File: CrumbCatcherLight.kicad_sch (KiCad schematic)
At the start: 8 parts, among them J1 USB_C_Receptacle_USB2.0, U1 ECMF02-2AMX6

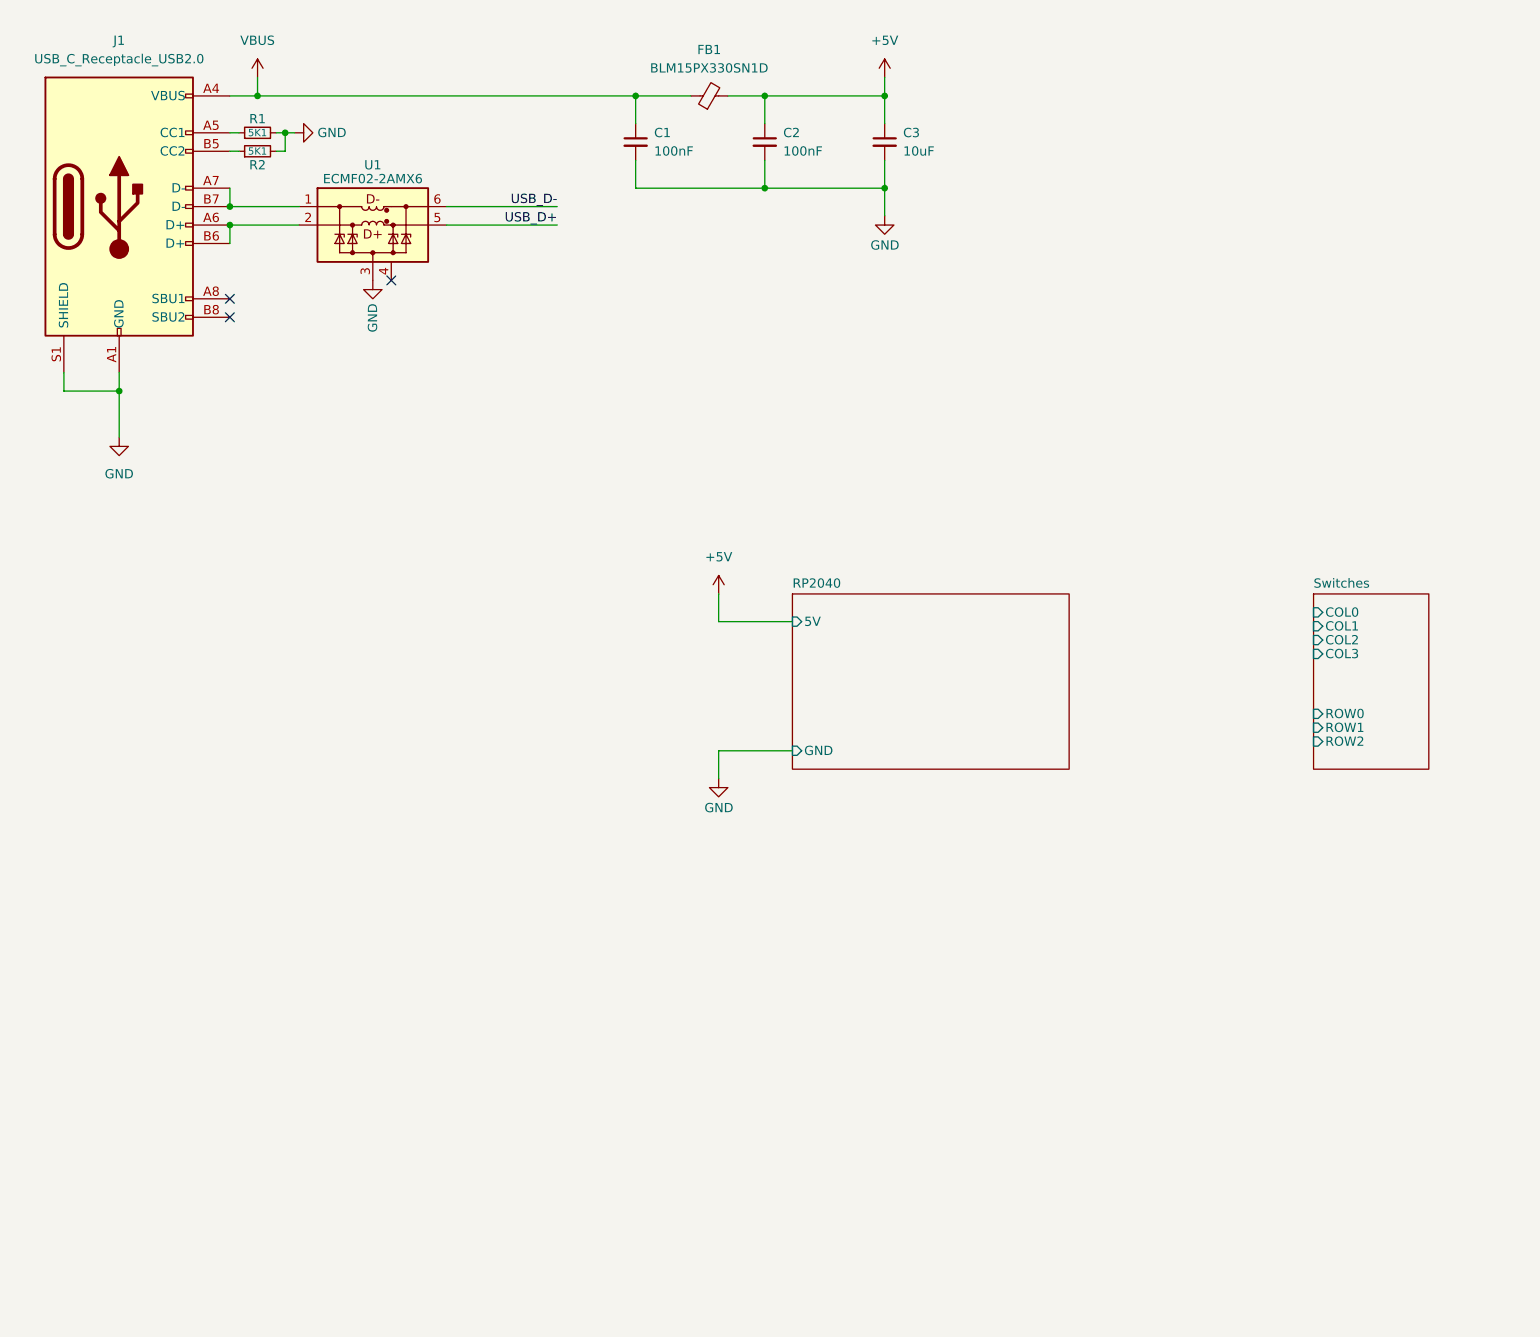
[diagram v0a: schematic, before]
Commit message: Update lib, finish off rotary encoder schematic, reselect diode for reset circuit
Update RP2040, rename bom only footprint, add mechanical footprint. Add PCB symbol
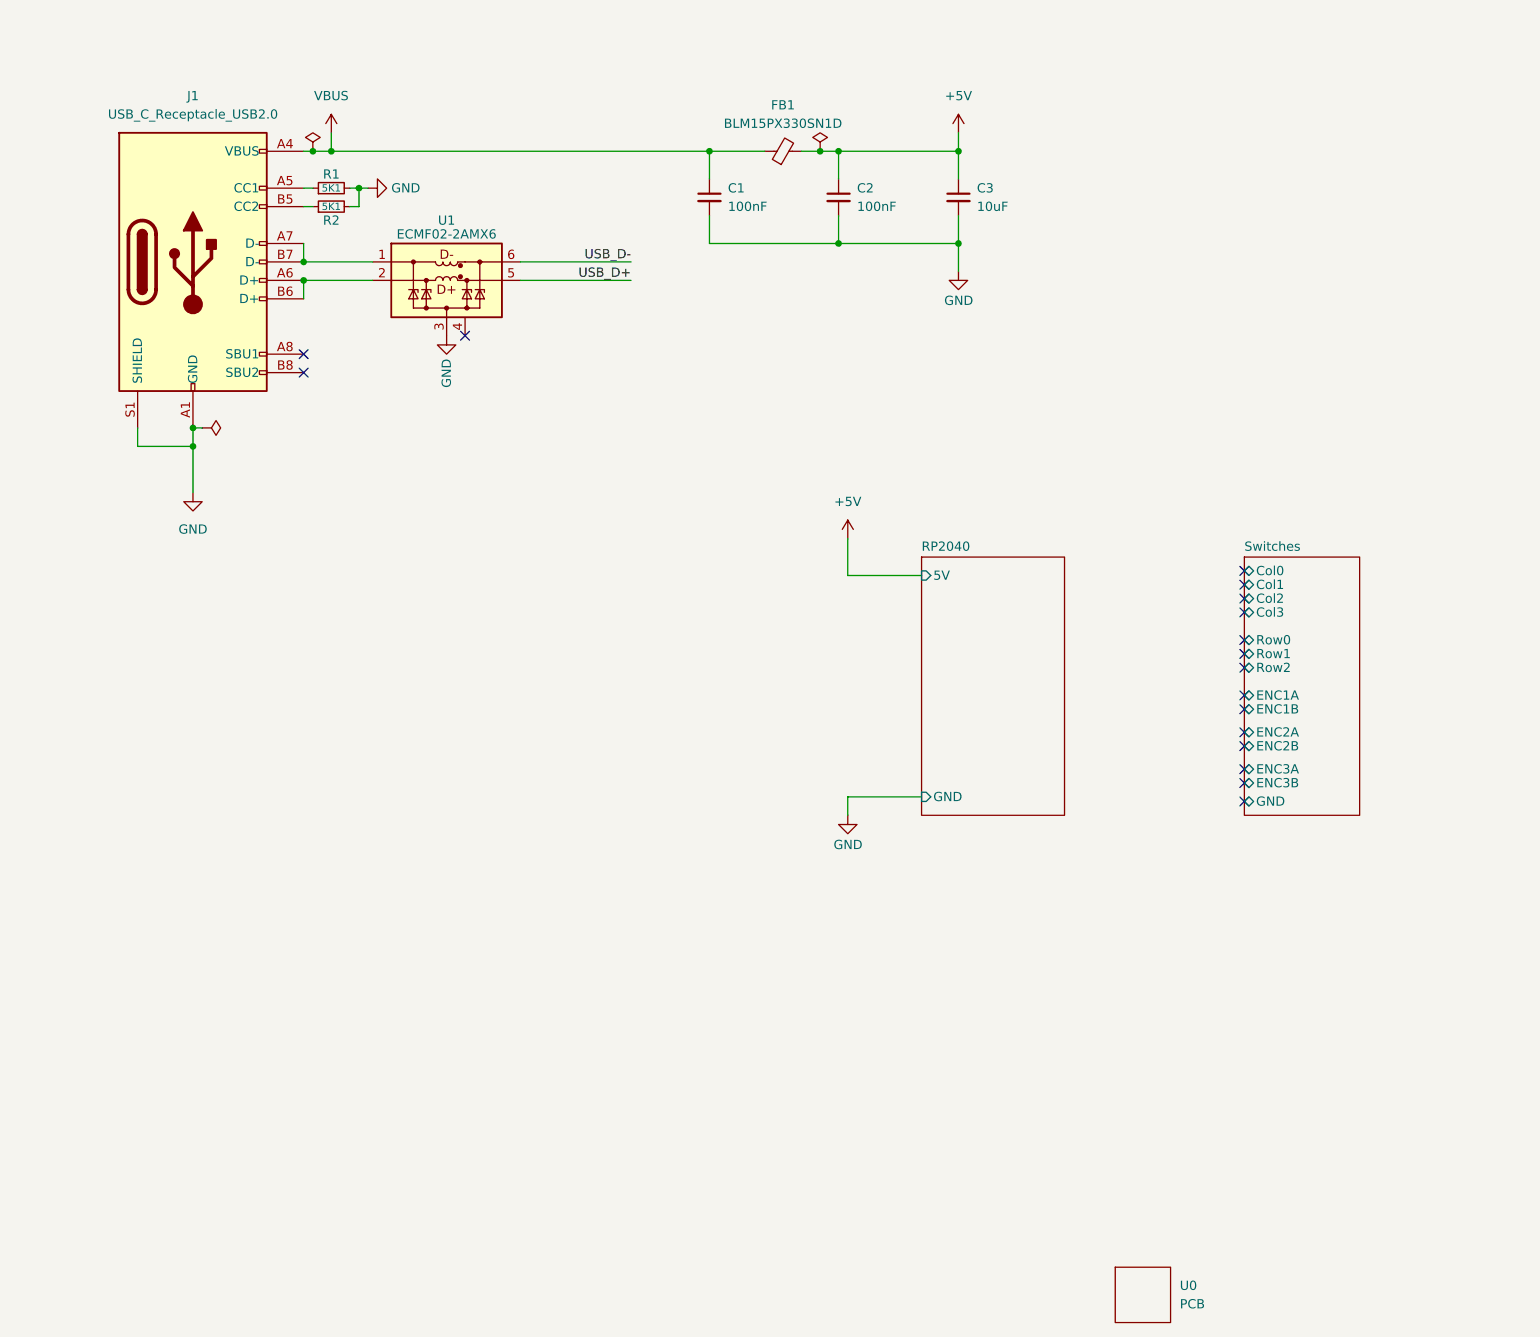
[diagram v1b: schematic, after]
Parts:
- added U0: PCB, Mad_Footprints:BOM, symbol Mad_Symbols:PCB
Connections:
- no-connect marks 3 -> 17
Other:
- sheet Switches ports: added Col0, Col1, Col2, Col3, ENC1A, ENC1B, ENC2A, ENC2B, ENC3A, ENC3B, GND, Row0, Row1, Row2; removed COL0, COL1, COL2, COL3, ROW0, ROW1, ROW2
- moved on the sheet: C1, C2, C3, FB1, J1, R1, R2, U1

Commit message: Finish off rotary encoders, add EMC zone for USB, fix few remaining lib links, fix DRC
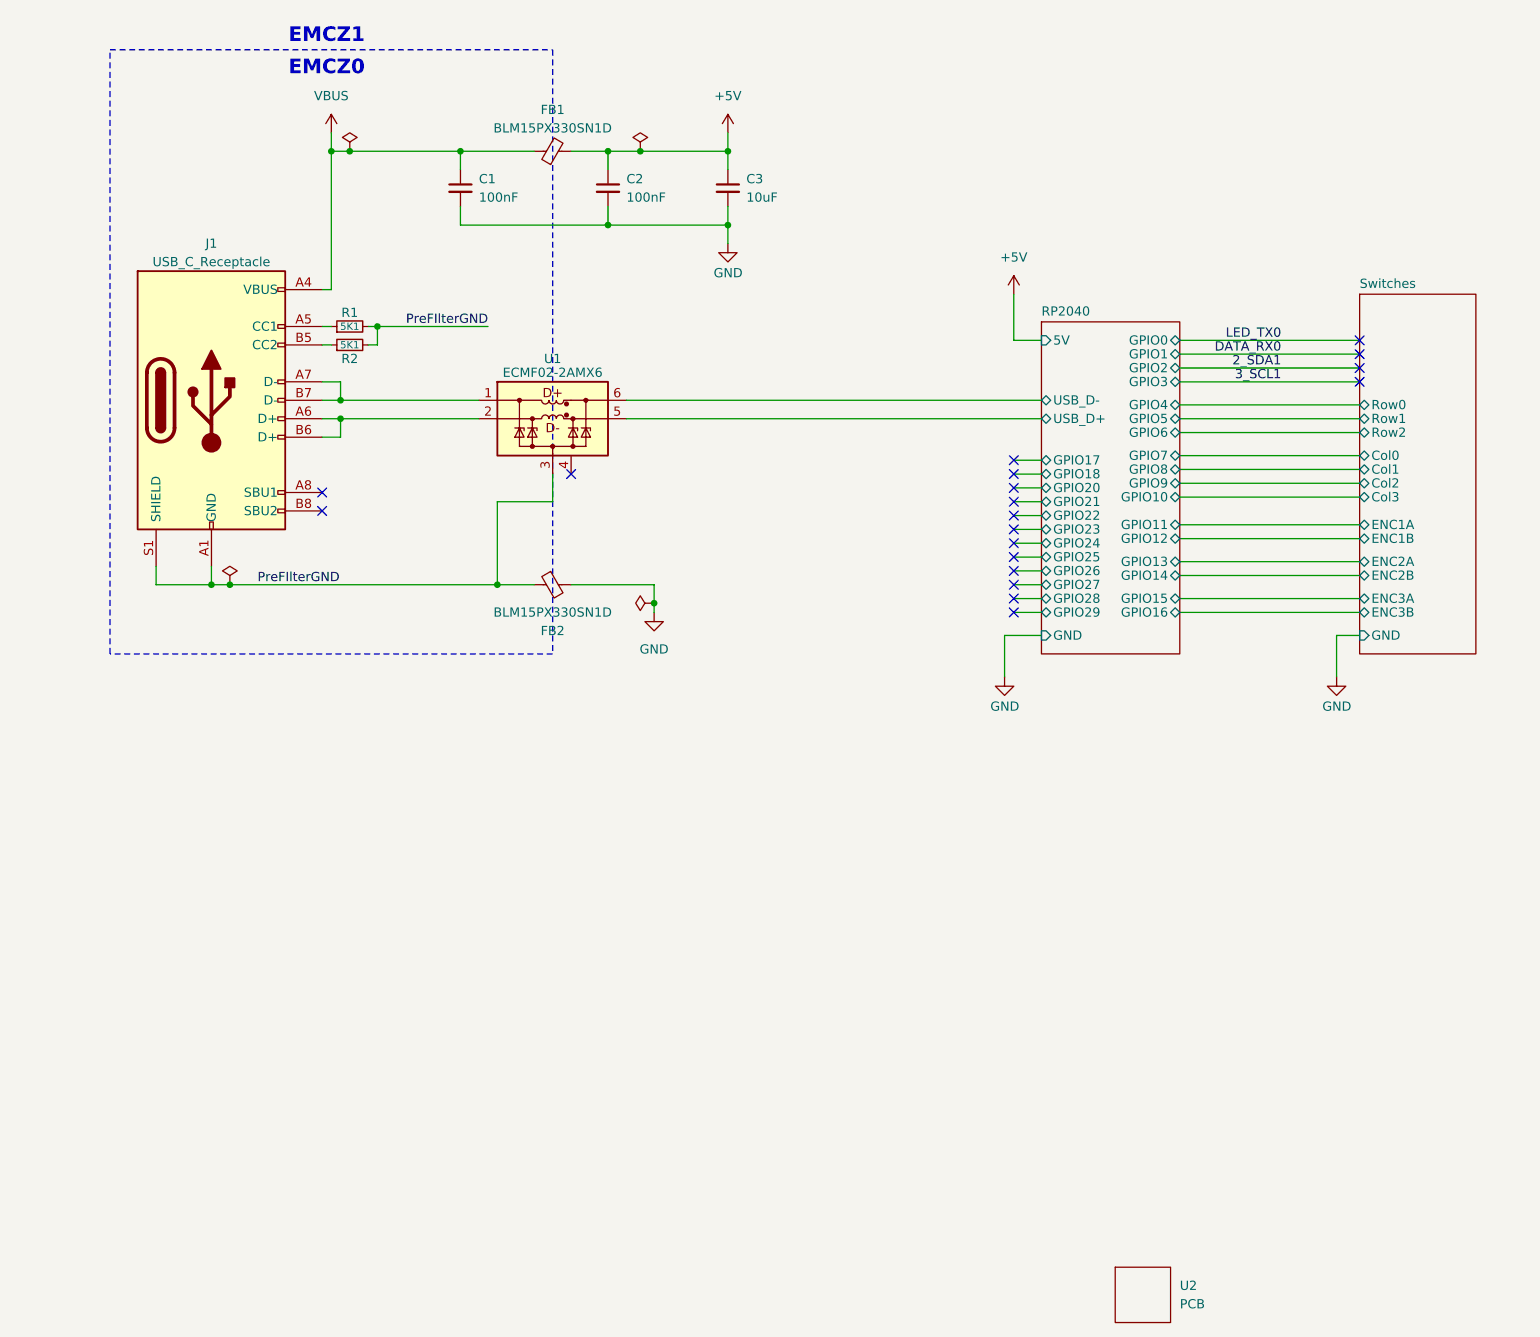
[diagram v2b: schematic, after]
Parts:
- added FB2: BLM15PX330SN1D, Inductor_SMD:L_0402_1005Metric, symbol Device:FerriteBead_Small
- J1: value USB_C_Receptacle_USB2.0 -> USB_C_Receptacle; symbol Connector:USB_C_Receptacle_USB2.0 -> Connector:USB_C_Receptacle_USB2.0_16P
- U1: symbol Local:ECMF02-2AMX6 -> Power_Protection:ECMF02-2AMX6
- renumbered U0 to U2
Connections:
- net GND: now also FB2.2; no longer J1.A1 (GND), J1.A12 (GND), J1.B1 (GND), J1.B12 (GND), J1.S1 (SHIELD), R1.2, R2.2, U1.3 (GND)
- net USB_D+ renamed RP2040/USB_D+
- net USB_D- renamed RP2040/USB_D-
- new net PreFIlterGND: FB2.1, J1.A1 (GND), J1.A12 (GND), J1.B1 (GND), J1.B12 (GND), J1.S1 (SHIELD), R1.2, R2.2, U1.3 (GND)
- no-connect marks 17 -> 19
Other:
- sheet RP2040 ports: added GPIO0, GPIO1, GPIO10, GPIO11, GPIO12, GPIO13, GPIO14, GPIO15, GPIO16, GPIO17, GPIO18, GPIO2, GPIO20, GPIO21, GPIO22, GPIO23, GPIO24, GPIO25, GPIO26, GPIO27, GPIO28, GPIO29, GPIO3, GPIO4, GPIO5, GPIO6, GPIO7, GPIO8, GPIO9, USB_D+, USB_D-; removed none
- note added: "EMCZ0"
- note added: "EMCZ1"
- moved on the sheet: C1, C2, C3, FB1, J1, R1, R2, U1

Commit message: Refactor, cleanup, add todo list, update metadata on BOM
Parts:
- removed C1, C2: 100nF, Capacitor_SMD:C_0402_1005Metric, symbol Device:C_Small
- removed C3: 10uF, Capacitor_SMD:C_0402_1005Metric, symbol Device:C_Small
- removed FB1, FB2: BLM15PX330SN1D, Inductor_SMD:L_0402_1005Metric, symbol Device:FerriteBead_Small
- removed J1: USB_C_Receptacle, Connector_USB:USB_C_Receptacle_GCT_USB4105-xx-A_16P_TopMnt_Horizontal, symbol Connector:USB_C_Receptacle_USB2.0_16P
- removed R1, R2: 5K1, Resistor_SMD:R_0402_1005Metric, symbol Device:R_Small
- removed U1: ECMF02-2AMX6, Package_DFN_QFN:ST_UQFN-6L_1.5x1.7mm_P0.5mm, symbol Power_Protection:ECMF02-2AMX6
- renumbered U2 to U0
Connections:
- no-connect marks 19 -> 16
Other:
- sheet RP2040 ports: added none; removed 5V, USB_D+, USB_D-
- sheet Switches ports: added 5V, DIN, DOUT; removed none
- note added: "TODO: * Finish the RP2040 controller refactor. * Pull out what we need for the rotary Encoders * Add Status LED to RP2040 * Cleanup * DRC/ERC"
- note removed: "EMCZ0"
- note removed: "EMCZ1"

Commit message: Update BOM,
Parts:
- added C1, C2: 100nF, Capacitor_SMD:C_0402_1005Metric, symbol Device:C_Small
- added C3: 10uF, Capacitor_SMD:C_0805_2012Metric, symbol Device:C_Small
- added FB1, FB2: BLM15PX330SN1D, Inductor_SMD:L_0402_1005Metric, symbol Device:FerriteBead_Small
- added J1: USB_C_Receptacle, Connector_USB:USB_C_Receptacle_GCT_USB4105-xx-A_16P_TopMnt_Horizontal, symbol Connector:USB_C_Receptacle_USB2.0_16P
- added R1, R2: 5K1, Resistor_SMD:R_0402_1005Metric, symbol Device:R_Small
- added U1: ECMF02-2AMX6, Package_DFN_QFN:ST_UQFN-6L_1.5x1.7mm_P0.5mm, symbol Power_Protection:ECMF02-2AMX6
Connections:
- net GND: now also C2.2, C3.2, FB2.2
- new net: J1.A5 (CC1), R1.1
- new net: J1.A6 (D+), J1.B6 (D+), U1.2 (D-_in)
- new net: J1.A7 (D-), J1.B7 (D-), U1.1 (D+_in)
- new net: J1.B5 (CC2), R2.1
- new net +5V: C2.1, C3.1, FB1.2
- new net PreFIlterGND: C1.2, FB2.1, J1.A1 (GND), J1.A12 (GND), J1.B1 (GND), J1.B12 (GND), J1.S1 (SHIELD), R1.2, R2.2, U1.3 (GND)
- new net RP2040a/USB_D+: U1.6 (D+_out)
- new net RP2040a/USB_D-: U1.5 (D-_out)
- new net VBUS: C1.1, FB1.1, J1.A4 (VBUS), J1.A9 (VBUS), J1.B4 (VBUS), J1.B9 (VBUS)
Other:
- removed sheet RP2040
- added sheet RP2040a (mad_lib/schematics/Keyboard Controllers/RP2040.kicad_sch)
- sheet Switches ports: added none; removed Col3
- note added: "EMCZ0"
- note added: "EMCZ1"

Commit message: update madlib, add todo
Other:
- sheet RP2040a renamed RP2040
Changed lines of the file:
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@@
 			(color 0 0 0 0.0000)
 		)
-		(property "Sheetname" "RP2040a"
+		(property "Sheetname" "RP2040"
 			(at 153.67 57.7084 0)
 			(effects
